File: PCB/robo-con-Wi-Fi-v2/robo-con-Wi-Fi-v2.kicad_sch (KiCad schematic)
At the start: 107 parts, among them J1 Conn_01x04, J2 SMA-J, J3 Conn_01x05, J4 Conn_01x01, J5 Conn_01x02, J6 Conn_01x01, J7 Conn_01x06, J8 Conn_01x01, J9 Conn_01x01, SW1 SW_Push, SW2 SW_Slide, U1 STM32H723VGTx, U10 MCP73831-2-OT, U11 LM66100DCK, U15 LM66100DCK, U18 USB_Type-C, U2 LBEE5HY2FY, U3 FT234XD, U4 MCP1727-1802xMF, U5 RKJXV122400R, U6 LD39200PU33R, U7 RKJXV122400R, U8 TMHU28, U9 TMHU28, Y2 XRCGB25M000FFS1AR0

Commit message: PCB
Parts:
- added D2, D4: ESD, Diode_SMD:D_0603_1608Metric_Pad1.05x0.95mm_HandSolder, symbol Device:D_TVS_Small
- C82: value 1u -> 10u; footprint Capacitor_SMD:C_0402_1005Metric_Pad0.74x0.62mm_HandSolder -> Capacitor_SMD:C_0603_1608Metric_Pad1.08x0.95mm_HandSolder
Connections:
- net Serial_RX is gone; now on net Serial_TXD: U3.7 (TXD/D0)
- net Serial_TX is gone; now on net Serial_RXD: U3.10 (RXD/D1)
- net BT_UART_CTS: now also U1.71 (PA12)
- net BT_UART_RTS: now also U1.70 (PA11)
- net BT_UART_RXD: now also U1.68 (PA9)
- net BT_UART_TXD: now also U1.69 (PA10)
- net GND: now also D2.1 (A1), D4.1 (A1)
- net Serial_CTS: now also U1.59 (PD12), U3.11 (~{CTS}/D3); no longer U3.8 (~{RTS}/D2)
- net Serial_RTS: now also U1.58 (PD11), U3.8 (~{RTS}/D2); no longer U3.11 (~{CTS}/D3)
- net at R3.1, U18.A7 (D-), U18.B7 (D-): now also D2.2 (A2)
- net Serial_RXD: now reaches U1.55 (PD8)
- net Serial_TXD: now reaches U1.56 (PD9)
- net at R5.1, U18.A6 (D+), U18.B6 (D+): now also D4.2 (A2)
- no-connect marks 29 -> 35
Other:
- moved on the sheet: C12, C13, C16, C83, R3, R39, R40, R5, U11

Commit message: v2 配線
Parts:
- removed R1, R31: WA04X102, My_Library:WA04X102, symbol My_Library:WA04X102
- removed R28, R29: 10k, Resistor_SMD:R_0603_1608Metric_Pad0.98x0.95mm_HandSolder, symbol Device:R_Small
- removed R30, R47, R7: 1k, Resistor_SMD:R_0402_1005Metric_Pad0.72x0.64mm_HandSolder, symbol Device:R_Small
- added D15: W, Diode_SMD:D_0603_1608Metric_Pad1.05x0.95mm_HandSolder, symbol Device:LED_Small
- added D17: O, Diode_SMD:D_0603_1608Metric_Pad1.05x0.95mm_HandSolder, symbol Device:LED_Small
- added D18: R, Diode_SMD:D_0603_1608Metric_Pad1.05x0.95mm_HandSolder, symbol Device:LED_Small
- added R12, R13, R14, R15: 10k, Resistor_SMD:R_0402_1005Metric_Pad0.72x0.64mm_HandSolder, symbol Device:R_Small
- added R22, R34, R36: 1k, Resistor_SMD:R_0402_1005Metric_Pad0.72x0.64mm_HandSolder, symbol Device:R_Small
- F1: value box -> FHC16322ADTP
- SW2: value SW_Slide -> SS-12D00G3
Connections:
- net L1_BUTTON is gone; now on net R1_BUTTON: J7.2 (Pin_2)
- net L2_BUTTON is gone; now on net R2_BUTTON: J7.3 (Pin_3)
- net L3_BUTTON is gone; now on net R3_BUTTON: J7.4 (Pin_4)
- net L4_BUTTON is gone; now on net R4_BUTTON: J7.5 (Pin_5)
- net R5_BUTTON is gone; now on net L5_BUTTON: J3.2 (Pin_2)
- net R6_BUTTON is gone; now on net L6_BUTTON: J3.3 (Pin_3)
- net R7_BUTTON is gone; now on net L7_BUTTON: J3.4 (Pin_4)
- net +3.3V: now also D1.2 (A), D10.2 (A), D13.2 (A), D14.2 (A), D16.2 (A), D3.2 (A), D5.2 (A), D17.2 (A), D18.2 (A); no longer R11.1, R2.1, R32.1, R33.1, R35.1, R4.1, R6.1
- net +5V: now also R22.1
- net BT_ON: now also U1.87 (PD6)
- net GND: now also D15.1 (K), R12.2, R13.2, R14.2, R15.2
- net L0_LEVER: now also U1.1 (PE2)
- net L1_LEVER: now also U1.3 (PE4)
- net L2_LEVER: now also U1.2 (PE3)
- net L3_LEVER: now also U1.4 (PE5)
- net L4_LEVER: now also U1.5 (PE6)
- net LED0: now also R2.2, U1.89 (PB3(JTDO); no longer D1.1 (K)
- net LED1: now also R4.2, U1.90 (PB4(NJTRST)); no longer D3.1 (K)
- net LED2: now also R6.2, U1.91 (PB5); no longer D5.1 (K)
- net LED3: now also R11.2, U1.92 (PB6); no longer D10.1 (K)
- net LED4: now also R32.2, U1.93 (PB7); no longer D13.1 (K)
- net LEDUSB: now also U1.96 (PB9), R34.2
- net LEDWL: now also R33.2, U1.95 (PB8); no longer D14.1 (K)
- net LP_STICK: now also U1.30 (PA6)
- net LX_STICK: now also U1.29 (PA5), R13.1
- net LY_STICK: now also U1.28 (PA4), R12.1
- net LiPo_OBSERVE: now also U1.33 (PC5)
- net R0_LEVER: now also U1.61 (PD14)
- net R1_LEVER: now also U1.63 (PC6)
- net R2_LEVER: now also U1.62 (PD15)
- net R3_LEVER: now also U1.60 (PD13)
- net R4_LEVER: now also U1.57 (PD10)
- net RP_STICK: now also U1.47 (PB11)
- net RX_STICK: now also U1.34 (PB0), R14.1
- net RY_STICK: now also U1.35 (PB1), R15.1
- net SDMMC1_CLK: now also R44.7; no longer R44.6
- net SDMMC1_CMD: now also R44.8; no longer R44.5
- net SDMMC1_D2: now also R44.5
- net SDMMC1_D3: now also R44.6; no longer R44.7
- net WL_ON: now also U1.86 (PD5)
- net R1_BUTTON: now reaches U1.51 (PB12)
- net R2_BUTTON: now reaches U1.52 (PB13)
- net R3_BUTTON: now reaches U1.53 (PB14)
- net R4_BUTTON: now reaches U1.54 (PB15)
- net L5_BUTTON: now reaches U1.7 (PC13)
- net L6_BUTTON: now reaches U1.8 (PC14)
- net L7_BUTTON: now reaches U1.9 (PC15)
- net LEDLiPo_GOOD: now reaches U1.97 (PE0)
- net LEDLiPo_GOOD: now also R35.2
- net LEDLiPo_BAD: now reaches U1.98 (PE1)
- net LEDLiPo_BAD: now also R36.2
- net LEDLiPo: no longer names the net of D16.1 (K)
- net LEDLiPo: now also R35.1
- new net: D13.1 (K), R32.1
- new net: D1.1 (K), R2.1
- new net: D3.1 (K), R4.1
- new net: D17.1 (K), R34.1
- new net: D18.1 (K), R36.1
- new net: D15.2 (A), R22.2
- new net: D5.1 (K), R6.1
- new net: D10.1 (K), R11.1
- new net: D14.1 (K), R33.1
- no-connect marks 35 -> 34
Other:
- moved on the sheet: D1, D10, D11, D13, D14, D16, D3, D5, J3, J7, R11, R2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

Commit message: PCB
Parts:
- removed J3: Conn_01x05, Connector_JST:JST_ZH_B5B-ZR_1x05_P1.50mm_Vertical, symbol Connector_Generic:Conn_01x05
- removed R12, R13, R14, R15: 10k, Resistor_SMD:R_0402_1005Metric_Pad0.72x0.64mm_HandSolder, symbol Device:R_Small
- added J10: Conn_01x06, Connector_JST:JST_ZH_B6B-ZR_1x06_P1.50mm_Vertical, symbol Connector_Generic:Conn_01x06
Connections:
- net +1V8: now also J10.1 (Pin_1)
- net GND: now also J10.6 (Pin_6)
- net L5_BUTTON: now also J10.2 (Pin_2)
- net L6_BUTTON: now also J10.3 (Pin_3)
- net L7_BUTTON: now also J10.4 (Pin_4)
- net L8_BUTTON: now reaches U1.15 (PC0)
- net L8_BUTTON: now also J10.5 (Pin_5)

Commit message: update
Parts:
- removed C57: 1u, Capacitor_SMD:C_0402_1005Metric_Pad0.74x0.62mm_HandSolder, symbol Device:C_Small
- removed C58, C67: 0.1u, Capacitor_SMD:C_0402_1005Metric_Pad0.74x0.62mm_HandSolder, symbol Device:C_Small
- removed SW2: SS-12D00G3, 0Ikedalibrary:swich_SS-12D00G3, symbol Switch:SW_Nidec_CAS-120A1
- removed U1: STM32H723VGTx, Package_QFP:LQFP-100_14x14mm_P0.5mm, symbol MCU_ST_STM32H7:STM32H723VGTx
- removed U8, U9: TMHU28, My_Library:TMHU28, symbol My_Library:TMHU28
- added SW3, SW4: SW_Push, My_Library:SKHHLPA010, symbol Switch:SW_Push
- added SW5: SW_Push_SPDT, My_Library:4MS1R202M6QES, symbol Switch:SW_Push_SPDT
- added SW6, SW7: SW_Push_SPDT, My_Library:8MS8P1B05VS2QES-C13, symbol Switch:SW_Push_SPDT
- added U8: STM32H7A3RGTx, Package_QFP:LQFP-64_10x10mm_P0.5mm, symbol MCU_ST_STM32H7:STM32H7A3RGTx
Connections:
- net +1V8: now also J10.6 (Pin_6), U8.1 (VBAT), U8.13 (VDDA), U8.19 (VDD), U8.32 (VDD), U8.48 (VDD), U8.64 (VDD); no longer J10.1 (Pin_1)
- net +3.3V: now also SW3.2, SW4.2, SW6.1 (A), SW7.1 (A)
- net +5V: now also SW5.1 (A)
- net BOOT0: now also U8.60 (BOOT0)
- net GND: now also J10.1 (Pin_1), SW5.3 (C), SW6.3 (C), SW7.3 (C), U8.12 (VSSA), U8.18 (VSS), U8.31 (VSS), U8.47 (VSS), U8.63 (VSS); no longer J10.6 (Pin_6)
- net HSE_IN: now also U8.5 (PH0)
- net HSE_OUT: now also U8.6 (PH1)
- net L5_BUTTON: now also J10.5 (Pin_5); no longer J10.2 (Pin_2)
- net L6_BUTTON: now also J10.4 (Pin_4); no longer J10.3 (Pin_3)
- net L7_BUTTON: now also J10.3 (Pin_3); no longer J10.4 (Pin_4)
- net L8_BUTTON: now also J10.2 (Pin_2); no longer J10.5 (Pin_5)
- net LDO_EN: now also SW5.2 (B)
- net NRST: now also U8.7 (NRST)
- net SDMMC1_CLK: now also U8.53 (PC12)
- net SDMMC1_CMD: now also U8.54 (PD2)
- net SDMMC1_D0: now also U8.34 (PB13)
- net SDMMC1_D1: now also U8.39 (PC9)
- net SDMMC1_D2: now also U8.51 (PC10)
- net SDMMC1_D3: now also U8.52 (PC11)
- net SWCLK: now also U8.49 (PA14)
- net SWDIO: now also U8.45 (PA13)
- net at C31.1, C50.1: now also U8.46 (VCAP)
- net at C30.1, C33.1: now also U8.30 (VCAP)
- new net L_PUSH: SW3.1
- new net L_PUSH_HOME: SW6.2 (B)
- new net R_PUSH: SW4.1
- new net R_PUSH_HOME: SW7.2 (B)
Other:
- moved on the sheet: C30, C31, C33, C50, C61, C66, C68, C69, C70, C71, C72, C73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

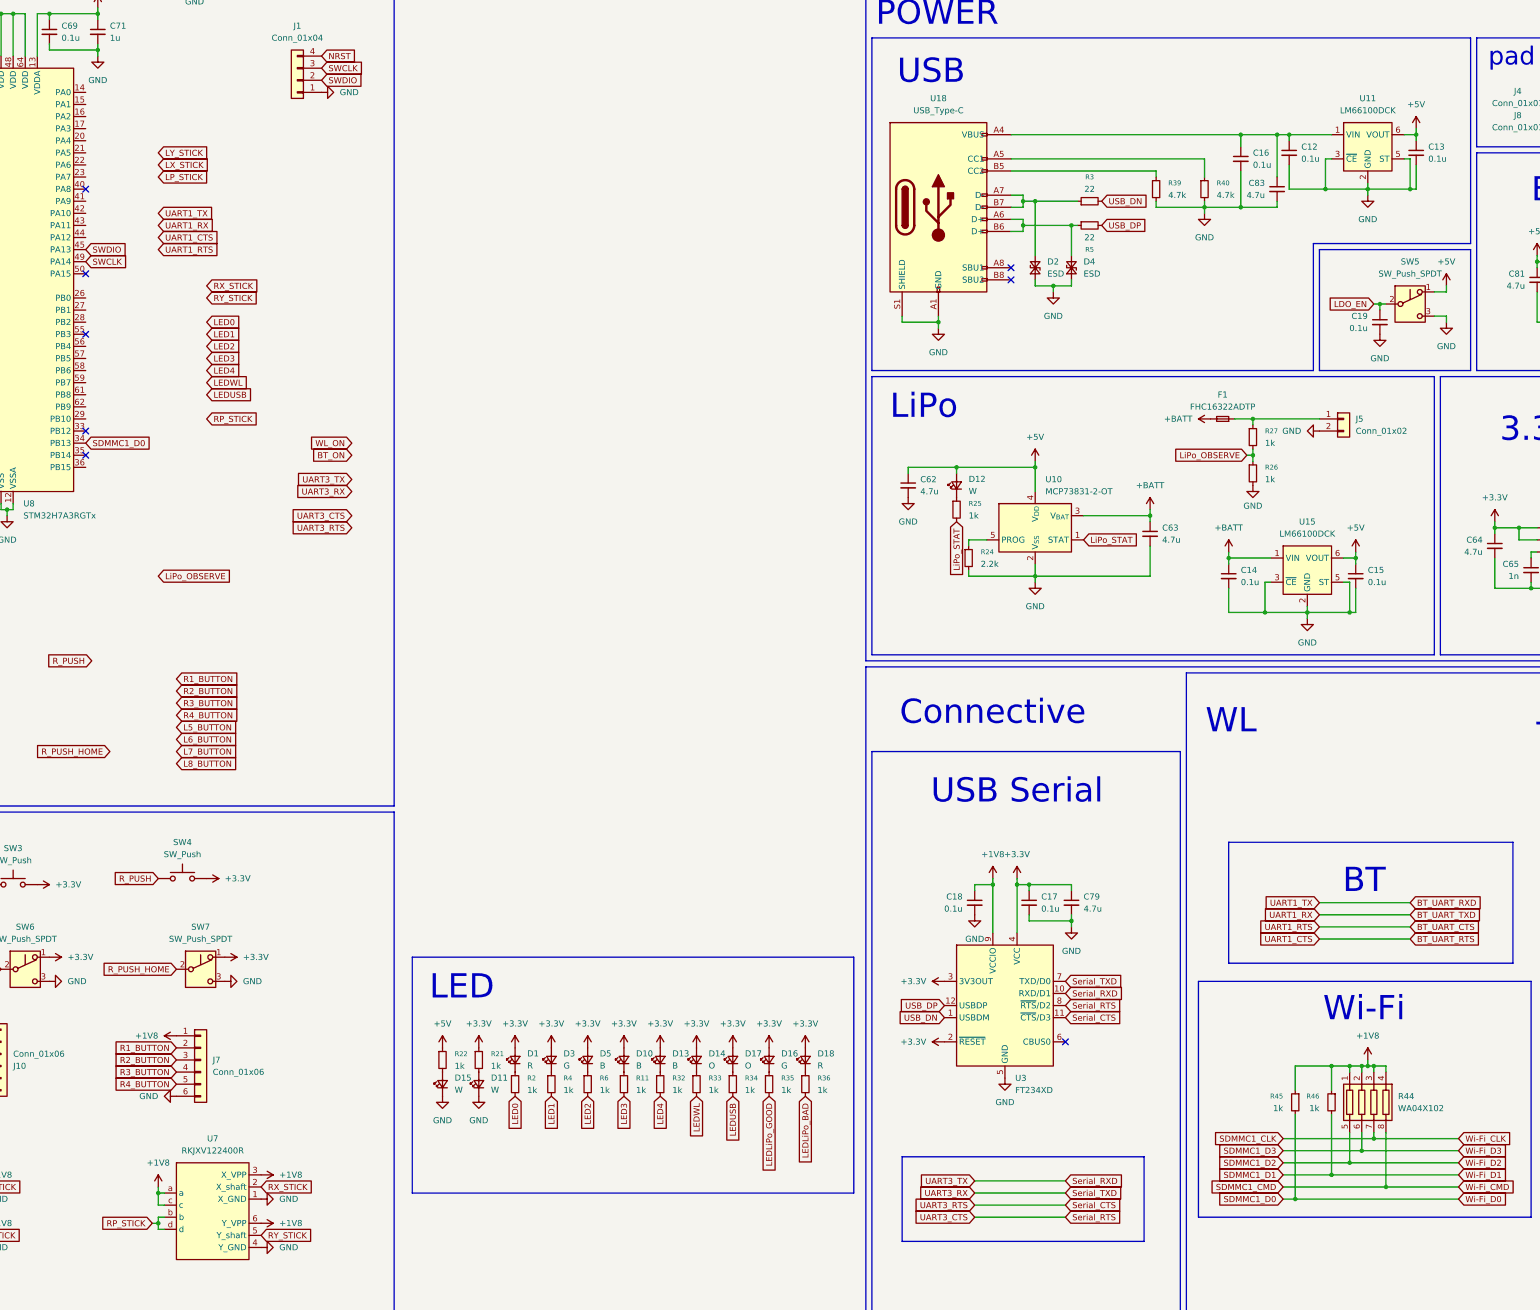
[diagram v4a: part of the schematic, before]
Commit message: move v2 program file & update PCB
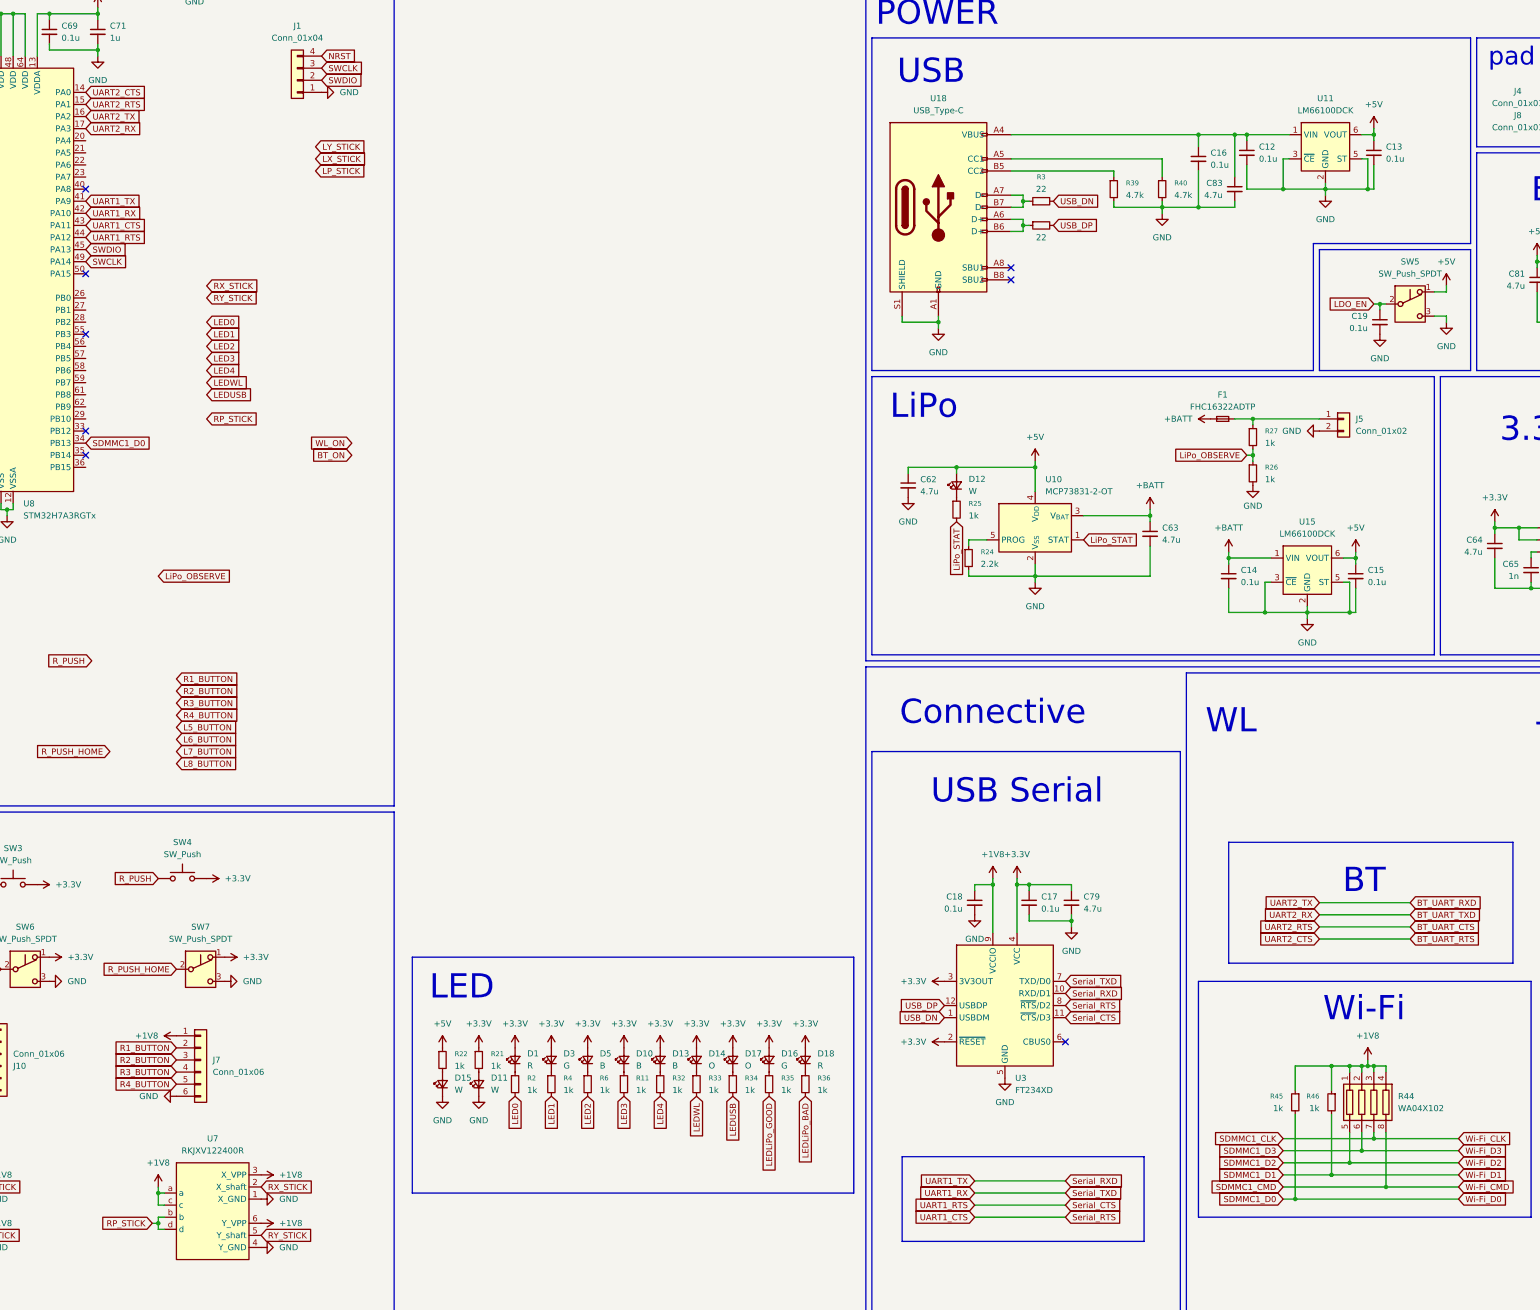
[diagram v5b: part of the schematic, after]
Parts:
- removed D2, D4: ESD, Diode_SMD:D_0603_1608Metric_Pad1.05x0.95mm_HandSolder, symbol Device:D_TVS_Small
- J1: footprint Connector_PinSocket_2.54mm:PinSocket_1x04_P2.54mm_Horizontal -> Connector_PinSocket_2.54mm:PinSocket_1x04_P2.54mm_Vertical
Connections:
- net BT_UART_CTS: now also U8.15 (PA1)
- net BT_UART_RTS: now also U8.14 (PA0)
- net BT_UART_RXD: now also U8.16 (PA2)
- net BT_UART_TXD: now also U8.17 (PA3)
- net Serial_CTS: now also U8.44 (PA12)
- net Serial_RTS: now also U8.43 (PA11)
- net Serial_RXD: now also U8.41 (PA9)
- net Serial_TXD: now also U8.42 (PA10)
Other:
- moved on the sheet: C12, C13, C16, C83, R3, R39, R40, U11

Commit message: update PCB
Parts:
- removed J10, J7: Conn_01x06, Connector_JST:JST_ZH_B6B-ZR_1x06_P1.50mm_Vertical, symbol Connector_Generic:Conn_01x06
- added J11, J3: Conn_01x05, Connector_JST:JST_ZH_B5B-ZR_1x05_P1.50mm_Vertical, symbol Connector_Generic:Conn_01x05
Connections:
- net +1V8: now also SW3.2, SW4.2, SW6.1 (A), SW7.1 (A), J11.1 (Pin_1), J3.5 (Pin_5)
- net +3.3V: no longer SW3.2, SW4.2, SW6.1 (A), SW7.1 (A)
- net L5_BUTTON: now also U8.59 (PB7), J3.4 (Pin_4)
- net L6_BUTTON: now also U8.58 (PB6), J3.3 (Pin_3)
- net L7_BUTTON: now also U8.57 (PB5), J3.2 (Pin_2)
- net L8_BUTTON: now also U8.56 (PB4), J3.1 (Pin_1)
- net LX_STICK: now also U8.9 (PC1)
- net LY_STICK: now also U8.8 (PC0)
- net L_PUSH: now also U8.62 (PB9)
- net L_PUSH_HOME: now also U8.61 (PB8)
- net LiPo_OBSERVE: now also U8.22 (PA6)
- net R1_BUTTON: now also U8.23 (PA7), J11.2 (Pin_2)
- net R2_BUTTON: now also U8.24 (PC4), J11.3 (Pin_3)
- net R3_BUTTON: now also U8.25 (PC5), J11.4 (Pin_4)
- net R4_BUTTON: now also U8.26 (PB0), J11.5 (Pin_5)
- net RX_STICK: now also U8.21 (PA5)
- net RY_STICK: now also U8.20 (PA4)
- net R_PUSH: now also U8.28 (PB2)
- net R_PUSH_HOME: now also U8.29 (PB10)
- net SDMMC1_CLK: now also R44.6; no longer R44.7
- net SDMMC1_CMD: now also R44.5; no longer R44.8
- net SDMMC1_D2: now also R44.8; no longer R44.5
- net SDMMC1_D3: now also R44.7; no longer R44.6

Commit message: update PCB
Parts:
- removed D15: W, Diode_SMD:D_0603_1608Metric_Pad1.05x0.95mm_HandSolder, symbol Device:LED_Small
- removed D18: R, Diode_SMD:D_0603_1608Metric_Pad1.05x0.95mm_HandSolder, symbol Device:LED_Small
- removed R22, R36: 1k, Resistor_SMD:R_0402_1005Metric_Pad0.72x0.64mm_HandSolder, symbol Device:R_Small
- D10, D13: value B -> O
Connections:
- net BT_ON: now also U8.36 (PB15)
- net LP_STICK: now also U8.2 (PC13)
- net RP_STICK: now also U8.27 (PB1)
- net WL_ON: now also U8.37 (PC6)
- net LED3 renamed LEDWLTX
- net LED4 renamed LEDWLRX
- net LEDLiPo_GOOD renamed LEDLiPo
- no-connect marks 34 -> 32
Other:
- moved on the sheet: D10, D13, D14, D17, R11, R32, R33, R34

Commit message: up
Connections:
- net LED0: now also U8.40 (PA8)
- net LED1: now also U8.50 (PA15)
- net LED2: now also U8.4 (PC15)
- net LEDLiPo: now also U8.33 (PB12)
- net LEDUSB: now also U8.55 (PB3)
- net LEDWL: now also U8.3 (PC14)
- net LEDWLRX: now also U8.10 (PC2)
- net LEDWLTX: now also U8.11 (PC3)
- no-connect marks 32 -> 30
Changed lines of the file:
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@@
 	)
 	(no_connect
-		(at 147.32 154.94)
-	)
-	(no_connect
 		(at 525.78 265.43)
 	)
@@
 	)
 	(no_connect
-		(at 147.32 104.14)
-	)
-	(no_connect
 		(at 525.78 289.56)
 	)
@@
 	(global_label "LED1"
 		(shape input)
-		(at 172.72 134.62 0)
+		(at 147.32 121.92 0)
 		(fields_autoplaced yes)
 		(effects
@@
 		)
 		(property "Intersheetrefs" "${INTERSHEET_REFS}"
-			(at 180.3618 134.62 0)
+			(at 156.2318 121.92 0)
 			(hide yes)
 			(show_name no)
@@
 	(global_label "LEDWLRX"
 		(shape input)
-		(at 172.72 151.13 0)
+		(at 111.76 111.76 180)
 		(fields_autoplaced yes)
 		(effects
@@
 				(size 1.27 1.27)
 			)
-			(justify left)
+			(justify right)
 		)
 		(property "Intersheetrefs" "${INTERSHEET_REFS}"
-			(at 180.3618 151.13 0)
+			(at 104.1182 111.76 0)
 			(hide yes)
 			(show_name no)
@@
 					(size 1.27 1.27)
 				)
-				(justify left)
+				(justify right)
 			)
 		)
@@
 	(global_label "LEDLiPo"
 		(shape input)
-		(at 187.96 115.57 180)
+		(at 147.32 154.94 0)
 		(fields_autoplaced yes)
 		(effects
@@
 				(size 1.27 1.27)
 			)
-			(justify right)
+			(justify left)
 		)
 		(property "Intersheetrefs" "${INTERSHEET_REFS}"
-			(at 177.4758 115.57 0)
+			(at 157.8042 154.94 0)
 			(hide yes)
 			(show_name no)
@@
 					(size 1.27 1.27)
 				)
-				(justify right)
+				(justify left)
 			)
 		)
@@
 	(global_label "LEDWLTX"
 		(shape input)
-		(at 172.72 153.67 0)
+		(at 111.76 114.3 180)
 		(fields_autoplaced yes)
 		(effects
@@
 				(size 1.27 1.27)
 			)
-			(justify left)
+			(justify right)
 		)
 		(property "Intersheetrefs" "${INTERSHEET_REFS}"
-			(at 180.3618 153.67 0)
+			(at 104.1182 114.3 0)
 			(hide yes)
 			(show_name no)
@@
 					(size 1.27 1.27)
 				)
-				(justify left)
+				(justify right)
 			)
 		)
@@
 	(global_label "LEDUSB"
 		(shape input)
-		(at 172.72 142.24 0)
+		(at 147.32 134.62 0)
 		(fields_autoplaced yes)
 		(effects
@@
 		)
 		(property "Intersheetrefs" "${INTERSHEET_REFS}"
-			(at 182.9623 142.24 0)
+			(at 157.5623 134.62 0)
 			(hide yes)
 			(show_name no)
@@
 	(global_label "LEDWL"
 		(shape input)
-		(at 172.72 139.7 0)
+		(at 111.76 139.7 180)
 		(fields_autoplaced yes)
 		(effects
@@
 				(size 1.27 1.27)
 			)
-			(justify left)
+			(justify right)
 		)
 		(property "Intersheetrefs" "${INTERSHEET_REFS}"
-			(at 181.6318 139.7 0)
+			(at 104.1182 139.7 0)
 			(hide yes)
 			(show_name no)
@@
 					(size 1.27 1.27)
 				)
-				(justify left)
+				(justify right)
 			)
 		)
@@
 	(global_label "LED0"
 		(shape input)
-		(at 172.72 132.08 0)
+		(at 147.32 104.14 0)
 		(fields_autoplaced yes)
 		(effects
@@
 		)
 		(property "Intersheetrefs" "${INTERSHEET_REFS}"
-			(at 180.3618 132.08 0)
+			(at 154.9618 104.14 0)
 			(hide yes)
 			(show_name no)
@@
 	(global_label "LED2"
 		(shape input)
-		(at 172.72 137.16 0)
+		(at 111.76 142.24 180)
 		(fields_autoplaced yes)
 		(effects
@@
 				(size 1.27 1.27)
 			)
-			(justify left)
+			(justify right)
 		)
 		(property "Intersheetrefs" "${INTERSHEET_REFS}"
-			(at 180.3618 137.16 0)
+			(at 104.1182 142.24 0)
 			(hide yes)
 			(show_name no)
@@
 					(size 1.27 1.27)
 				)
-				(justify left)
+				(justify right)
 			)
 		)
